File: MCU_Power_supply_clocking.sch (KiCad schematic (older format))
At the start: 60 parts, among them J2 OSTTC020162, J3 OSTTC020162, U10 TLV75529PDBV, U11 STM32H743ZIT6, U12 LD1117S33CTR, U13 LD1117S33CTR, U9 ST1L05APU33R, Y1 NX5032GA-8MHz, Y2 NX3215SA-32.768K-STD-MUA-14

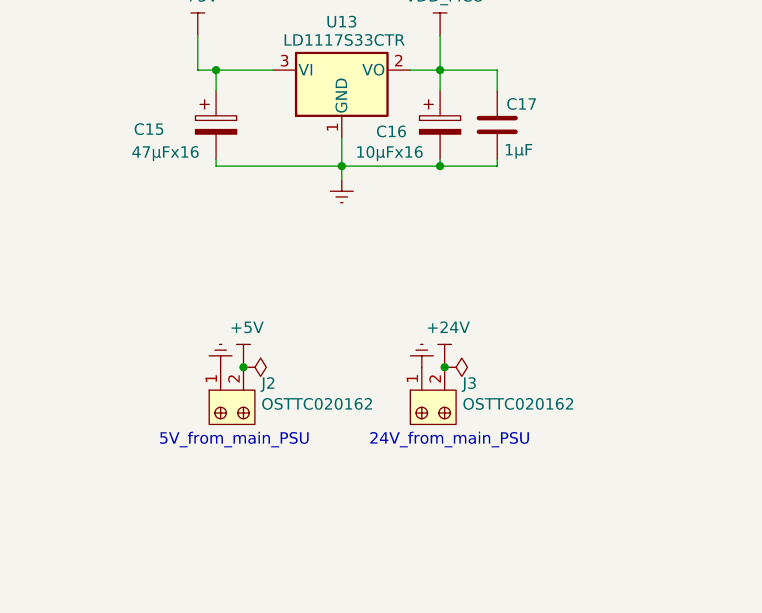
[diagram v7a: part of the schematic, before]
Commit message: Analog decoupling schema completed. Digital_IO completed and clean up
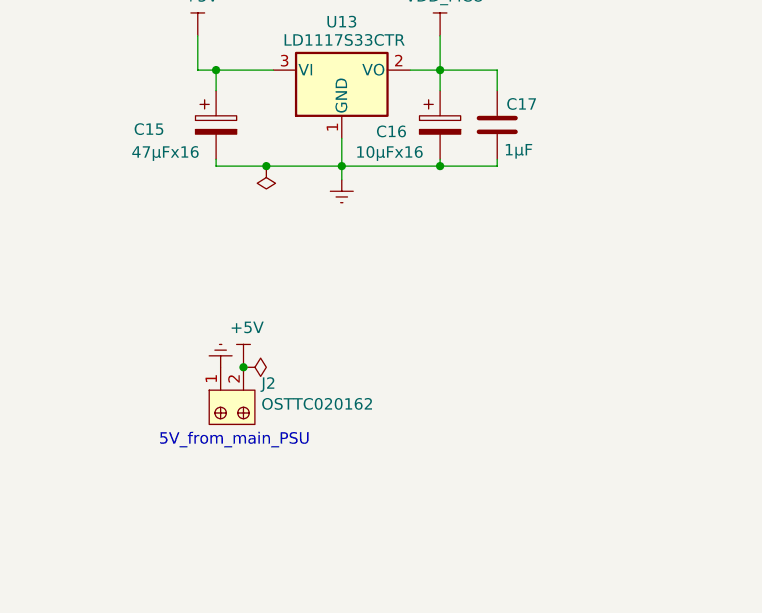
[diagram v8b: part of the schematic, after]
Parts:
- removed J3: OSTTC020162, digikey-footprints:Term_Block_1x2_P5mm, symbol dk_Terminal-Blocks-Wire-to-Board:OSTTC020162
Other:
- note removed: "24V_from_main_PSU"
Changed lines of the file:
@@
 	8140 5060 8140 5090
 Wire Wire Line
-	8140 5090 8690 5090
+	8140 5090 8360 5090
 Wire Wire Line
 	8690 5090 8690 4970
@@
 	2750 1250 3490 1250
 $Comp
-L dk_Terminal-Blocks-Wire-to-Board:OSTTC020162 J3
-U 1 1 60F32F26
-P 9040 6170
-F 0 "J3" H 9218 6299 50  0000 L CNN
-F 1 "OSTTC020162" H 9218 6208 50  0000 L CNN
-F 2 "digikey-footprints:Term_Block_1x2_P5mm" H 9240 6370 60  0001 L CNN
-F 3 "http://www.on-shore.com/wp-content/uploads/OSTTCXX0162.pdf" H 9240 6470 60  0001 L CNN
-F 4 "ED2600-ND" H 9240 6570 60  0001 L CNN "Digi-Key_PN"
-F 5 "OSTTC020162" H 9240 6670 60  0001 L CNN "MPN"
-F 6 "Connectors, Interconnects" H 9240 6770 60  0001 L CNN "Category"
-F 7 "Terminal Blocks - Wire to Board" H 9240 6870 60  0001 L CNN "Family"
-F 8 "http://www.on-shore.com/wp-content/uploads/OSTTCXX0162.pdf" H 9240 6970 60  0001 L CNN "DK_Datasheet_Link"
-F 9 "/product-detail/en/on-shore-technology-inc/OSTTC020162/ED2600-ND/614549" H 9240 7070 60  0001 L CNN "DK_Detail_Page"
-F 10 "TERM BLK 2POS SIDE ENTRY 5MM PCB" H 9240 7170 60  0001 L CNN "Description"
-F 11 "On Shore Technology Inc." H 9240 7270 60  0001 L CNN "Manufacturer"
-F 12 "Active" H 9240 7370 60  0001 L CNN "Status"
-	1    9040 6170
-	1    0    0    -1
-$EndComp
-$Comp
 L dk_Terminal-Blocks-Wire-to-Board:OSTTC020162 J2
 U 1 1 60F35197
@@
 Text Notes 7890 6320 0    50   ~ 0
 5V_from_main_PSU
-Text Notes 8810 6320 0    50   ~ 0
-24V_from_main_PSU
 $Comp
 L power:GNDREF #PWR?
@@
 $EndComp
 $Comp
-L power:GNDREF #PWR?
-U 1 1 60F37626
-P 9040 5970
-AR Path="/60F37626" Ref="#PWR?"  Part="1"
-AR Path="/60A03F8A/60F37626" Ref="#PWR047"  Part="1"
-F 0 "#PWR047" H 9040 5720 50  0001 C CNN
-F 1 "GNDREF" H 9045 5797 50  0001 C CNN
-F 2 "" H 9040 5970 50  0001 C CNN
-F 3 "" H 9040 5970 50  0001 C CNN
-	1    9040 5970
-	-1   0    0    1
-$EndComp
-$Comp
 L SVIELCOM_Library:+5V #PWR046
 U 1 1 60F37D7B
@@
 F 3 "" H 8260 5970 50  0001 C CNN
 	1    8260 5970
-	1    0    0    -1
-$EndComp
-$Comp
-L SVIELCOM_Library:+24V #PWR048
-U 1 1 60F390D1
-P 9140 5970
-F 0 "#PWR048" H 9290 6020 50  0001 C CNN
-F 1 "+24V" H 9155 6143 50  0000 C CNN
-F 2 "" H 9140 5970 50  0001 C CNN
-F 3 "" H 9140 5970 50  0001 C CNN
-	1    9140 5970
 	1    0    0    -1
 $EndComp
@@
 Connection ~ 8260 5970
 $Comp
-L power:PWR_FLAG #FLG08
-U 1 1 610E04FC
-P 9140 5970
-F 0 "#FLG08" H 9140 6045 50  0001 C CNN
-F 1 "PWR_FLAG" V 9140 6098 50  0001 L CNN
-F 2 "" H 9140 5970 50  0001 C CNN
-F 3 "~" H 9140 5970 50  0001 C CNN
-	1    9140 5970
-	0    1    1    0
-$EndComp
-Connection ~ 9140 5970
-$Comp
 L power:PWR_FLAG #FLG04
 U 1 1 61140523
@@
 Wire Wire Line
 	5030 5860 5150 5860
+$Comp
+L power:PWR_FLAG #FLG?
+U 1 1 60C26B49
+P 8360 5090
+F 0 "#FLG?" H 8360 5165 50  0001 C CNN
+F 1 "PWR_FLAG" V 8360 5218 50  0001 L CNN
+F 2 "" H 8360 5090 50  0001 C CNN
+F 3 "~" H 8360 5090 50  0001 C CNN
+	1    8360 5090
+	-1   0    0    1
+$EndComp
+Connection ~ 8360 5090
+Wire Wire Line
+	8360 5090 8690 5090
 $EndSCHEMATC
